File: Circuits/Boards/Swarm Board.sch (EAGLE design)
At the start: 81 parts, among them CON1 ISP(2X3), T1 NPN2N2222, T10 TEFT4300, T11 NPN2N2222, T12 NPN2N2222, T2 NPN2N2222, T3 NPN2N2222, T4 TEFT4300, T5 TEFT4300, T6 TEFT4300, T7 TEFT4300, T8 TEFT4300, T9 TEFT4300, U1 ATMEGA324P, U2 MCP73832SOT-23, U3 TB6552FN/FNG

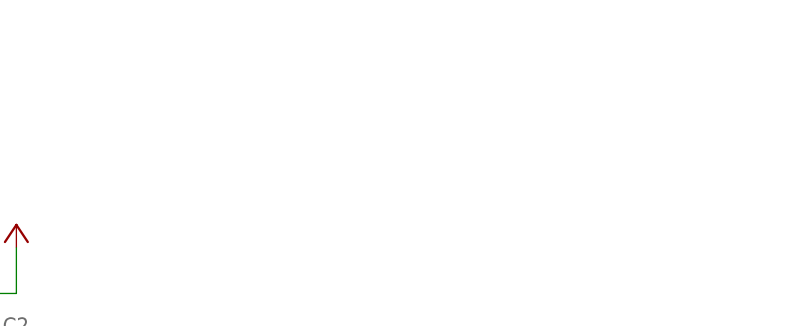
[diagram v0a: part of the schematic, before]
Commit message: 
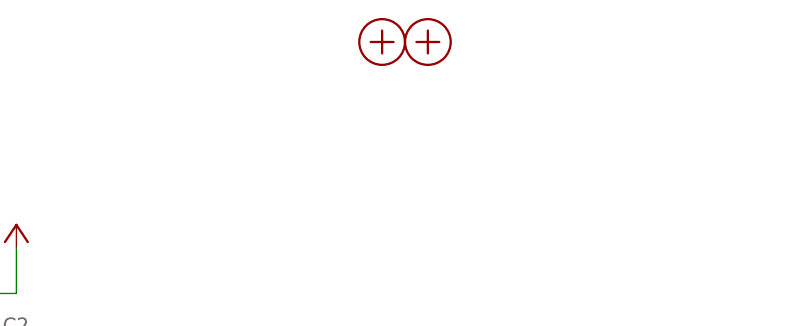
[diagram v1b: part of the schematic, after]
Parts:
- added H1, H2: MOUNTINGHOLE, Mechanical:MOUNTINGHOLE
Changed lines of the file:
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@@
 <part name="ANT2" library="Mechanical" deviceset="ANTENNA" device=""/>
 <part name="ANT3" library="Mechanical" deviceset="ANTENNA" device=""/>
+<part name="H1" library="Mechanical" deviceset="MOUNTINGHOLE" device=""/>
+<part name="H2" library="Mechanical" deviceset="MOUNTINGHOLE" device=""/>
 </parts>
 <sheets>
@@
 <instance part="ANT2" gate="G$1" x="-271.78" y="-55.88"/>
 <instance part="ANT3" gate="G$1" x="-271.78" y="-68.58"/>
+<instance part="H1" gate="G$1" x="91.44" y="129.54"/>
+<instance part="H2" gate="G$1" x="96.52" y="129.54"/>
 </instances>
 <busses>

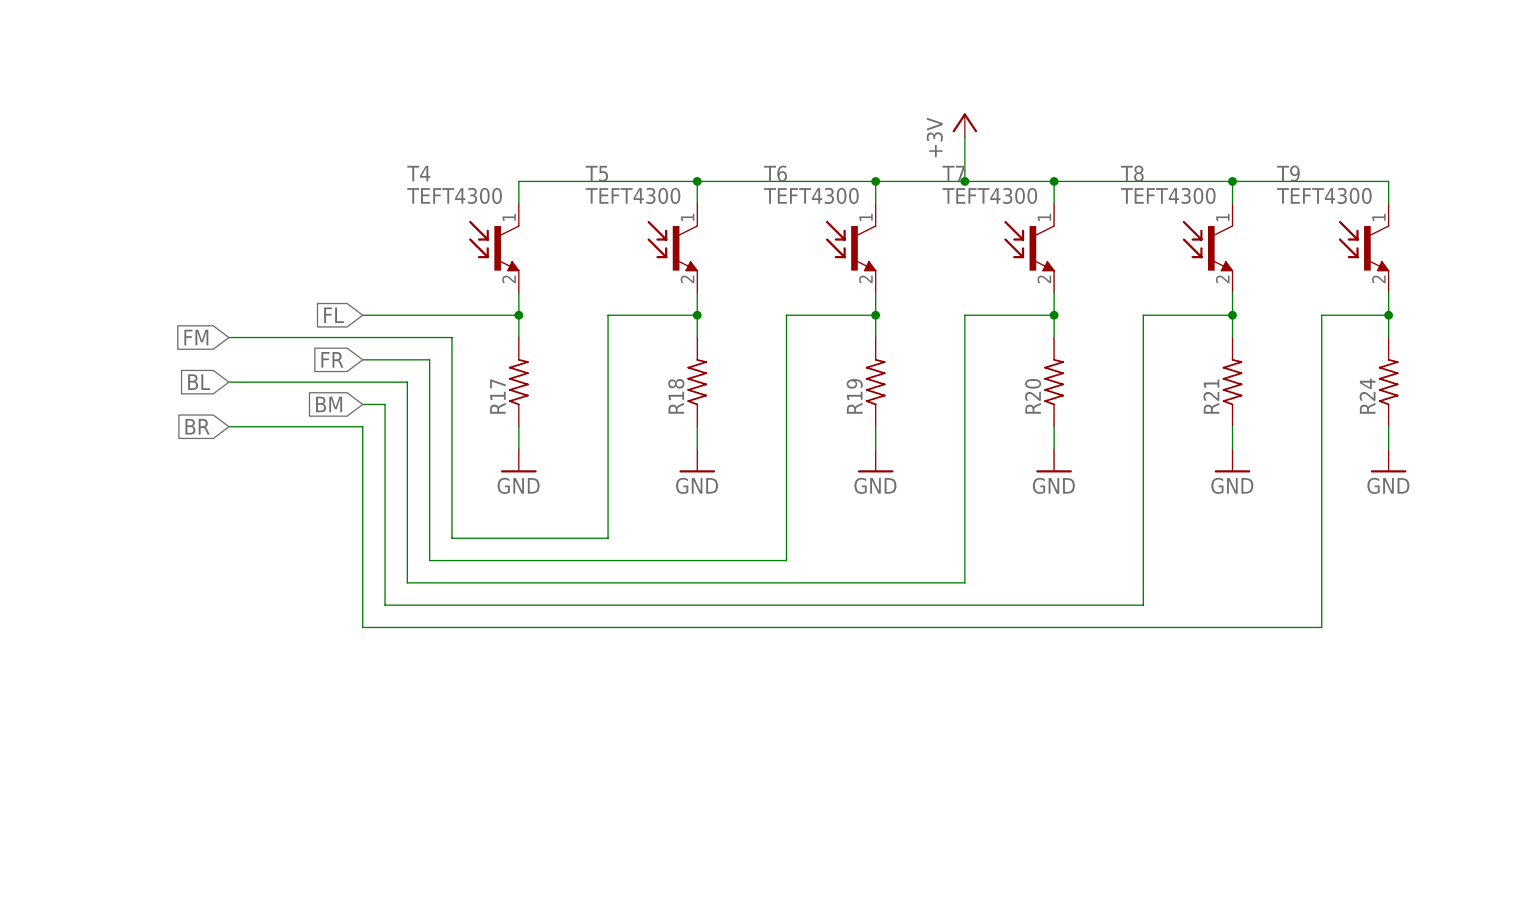
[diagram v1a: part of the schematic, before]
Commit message: 
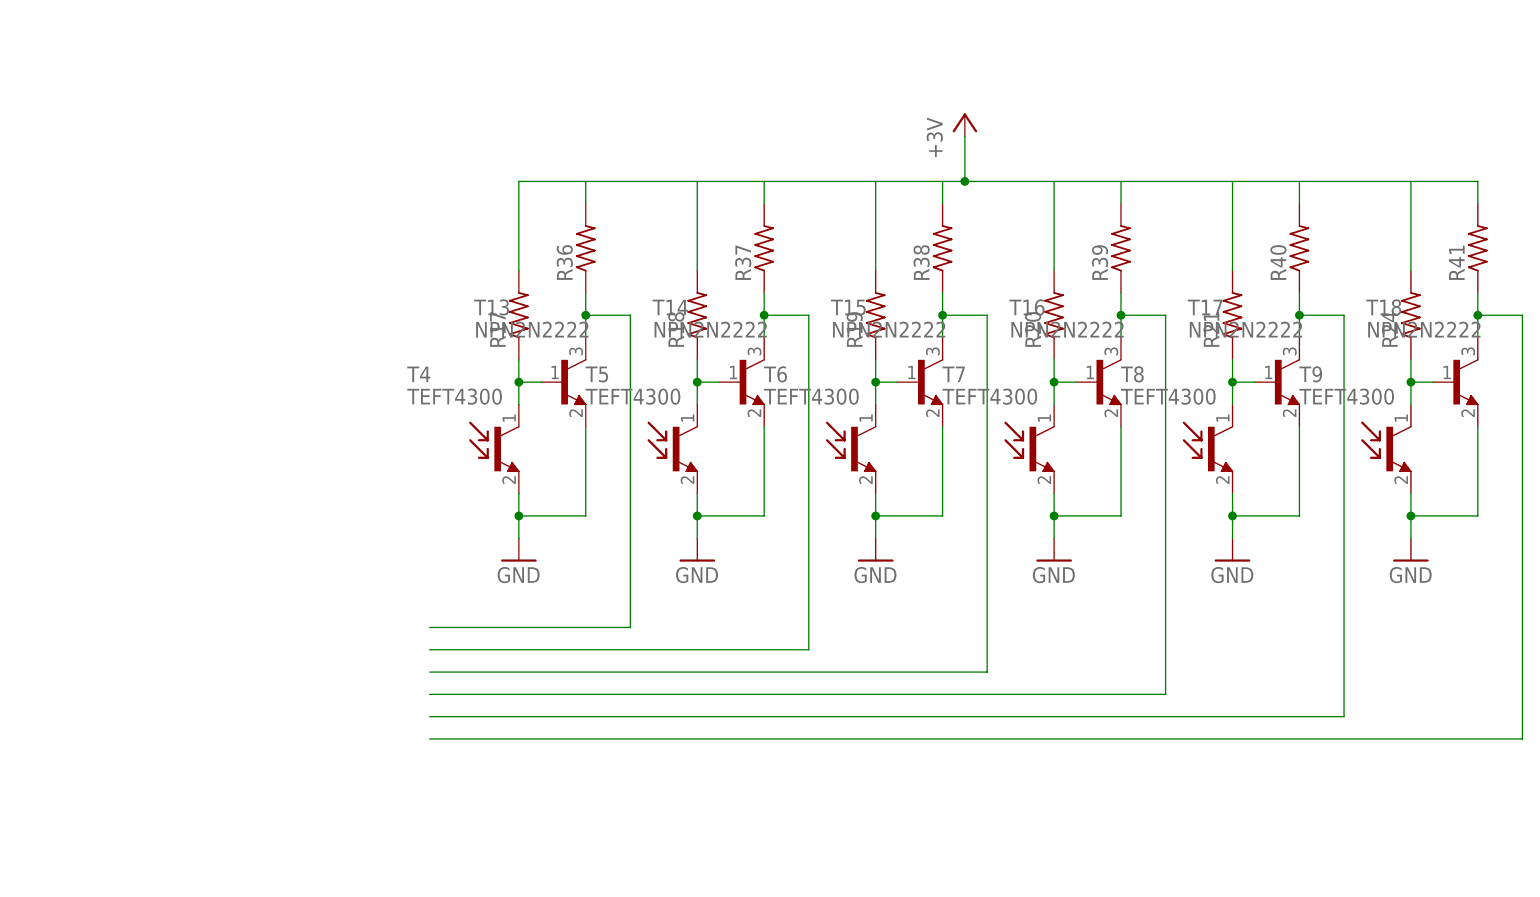
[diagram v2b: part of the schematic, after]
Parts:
- added R36, R37, R38, R39, R40, R41: (no value), Passive:RES0603
- added T13, T14, T15, T16, T17, T18: NPN2N2222, Passive:NPN2N2222
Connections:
- removed net BL: R20.2, T7.E
- removed net BM: R21.2, T8.E
- removed net BR: R24.2, T9.E
- removed net FL: R17.2, T4.E
- removed net FM: R18.2, T5.E
- removed net FR: R19.2, T6.E
- new net N$27: R17.1, T13.B, T4.C
- new net N$28: R36.1, T13.C
- new net N$29: R37.1, T14.C
- new net N$30: R38.1, T15.C
- new net N$31: R39.1, T16.C
- new net N$32: R40.1, T17.C
- new net N$33: R41.1, T18.C
- new net N$34: R24.1, T18.B, T9.C
- new net N$35: R21.1, T17.B, T8.C
- new net N$36: R20.1, T16.B, T7.C
- new net N$37: R19.1, T15.B, T6.C
- new net N$38: R18.1, T14.B, T5.C
- net +3V: now also R17.2, R18.2, R19.2, R20.2, R21.2, R24.2, R36.2, R37.2, R38.2, R39.2, R40.2, R41.2; no longer T4.C, T5.C, T6.C, T7.C, T8.C, T9.C
- net GND: now also T13.E, T14.E, T15.E, T16.E, T17.E, T18.E, T4.E, T5.E, T6.E, T7.E, T8.E, T9.E; no longer R17.1, R18.1, R19.1, R20.1, R21.1, R24.1
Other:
- moved on the sheet: R17, R18, R19, R20, R21, R24, T4, T5, T6, T7, T8, T9

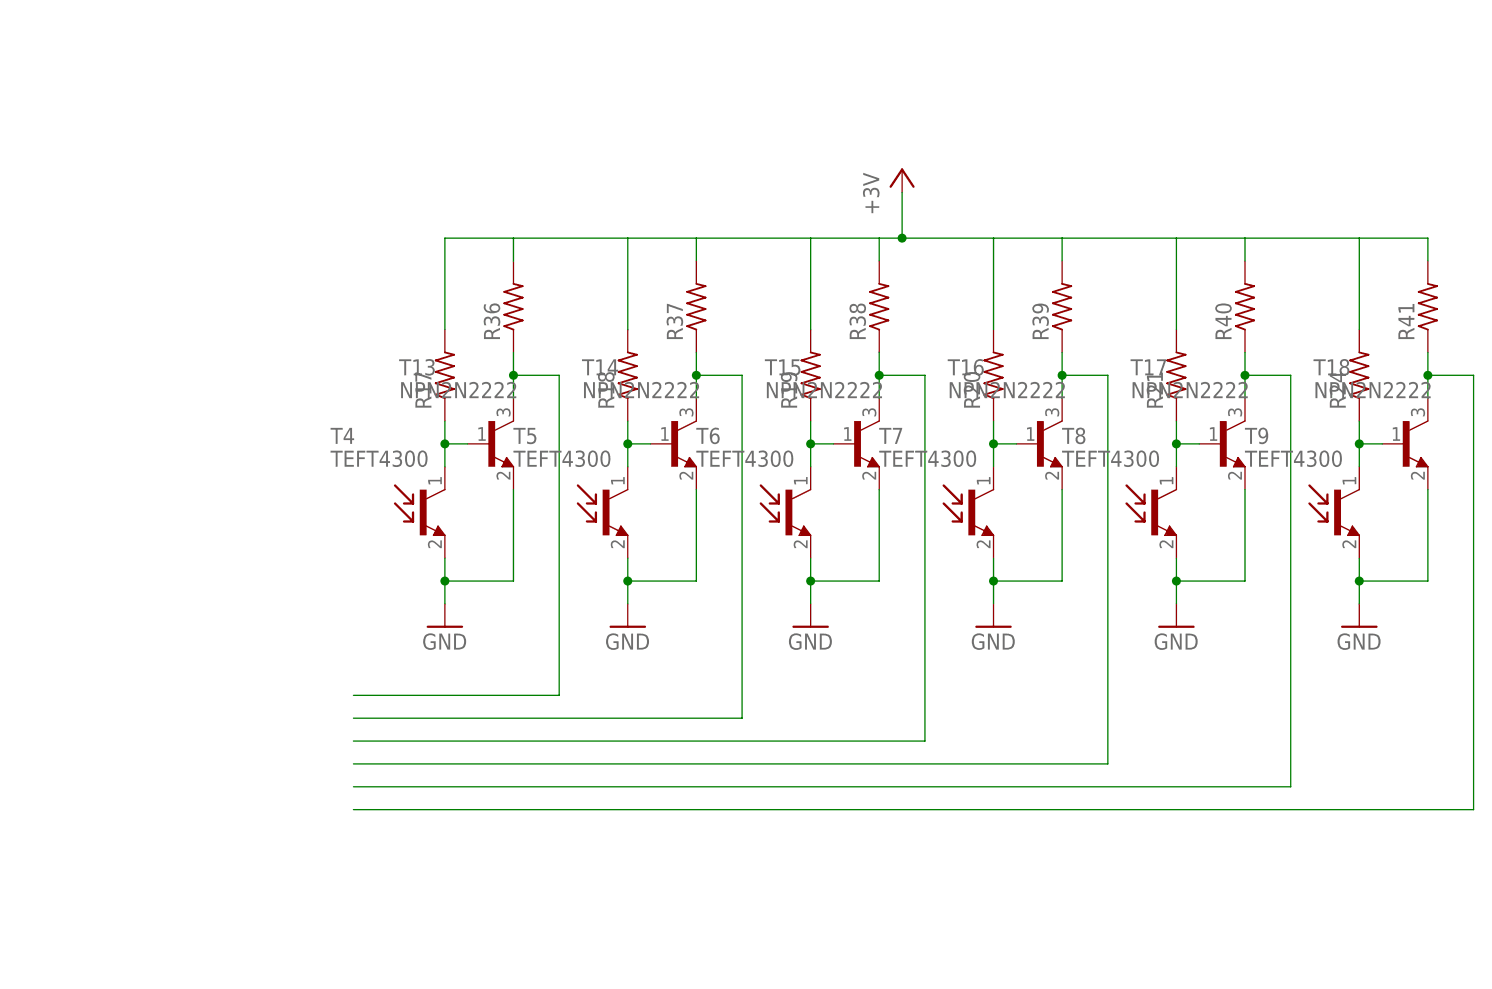
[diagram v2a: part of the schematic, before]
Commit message: 
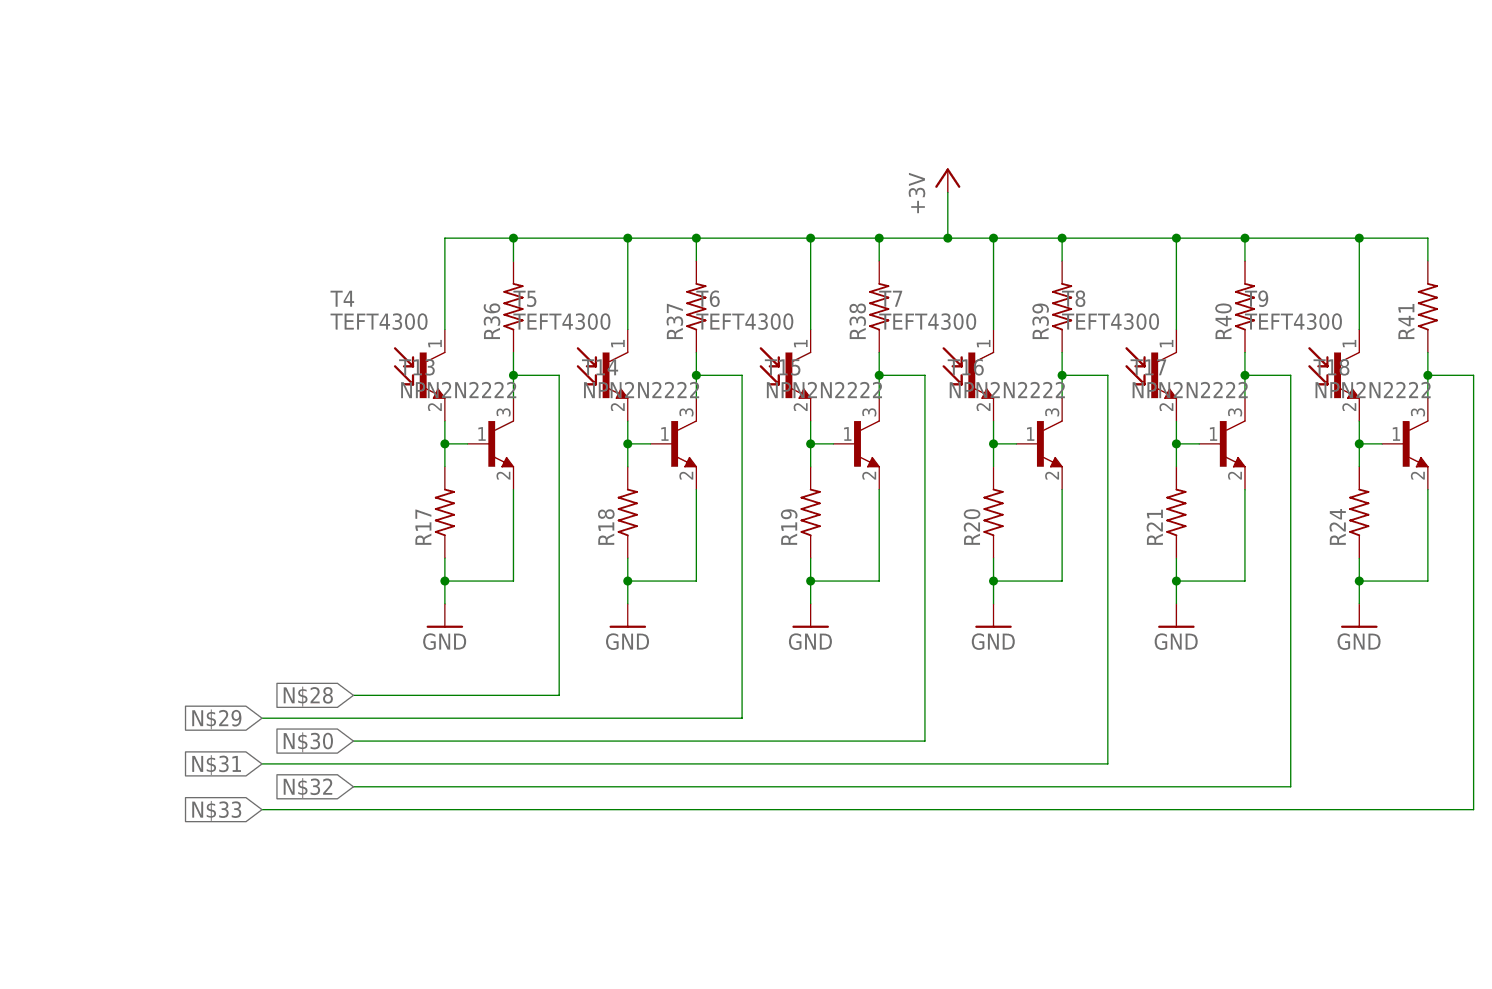
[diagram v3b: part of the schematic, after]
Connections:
- net +3V: now also T4.C, T5.C, T6.C, T7.C, T8.C, T9.C; no longer R17.2, R18.2, R19.2, R20.2, R21.2, R24.2
- net GND: now also R17.1, R18.1, R19.1, R20.1, R21.1, R24.1; no longer T4.E, T5.E, T6.E, T7.E, T8.E, T9.E
- net N$27: now also R17.2, T4.E; no longer R17.1, T4.C
- net N$34: now also R24.2, T9.E; no longer R24.1, T9.C
- net N$35: now also R21.2, T8.E; no longer R21.1, T8.C
- net N$36: now also R20.2, T7.E; no longer R20.1, T7.C
- net N$37: now also R19.2, T6.E; no longer R19.1, T6.C
- net N$38: now also R18.2, T5.E; no longer R18.1, T5.C
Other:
- moved on the sheet: R17, R18, R19, R20, R21, R24, T4, T5, T6, T7, T8, T9
